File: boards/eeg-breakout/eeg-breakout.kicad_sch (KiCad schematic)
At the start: 36 parts, among them J1 Isolated SPI, J2 Electrodes, U1 ISOW7741, U2 ADS1292IRSMR

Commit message: feat: tweak the eeg breakout
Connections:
- net +3V3: now also U2.31 (RESP_MODP/IN3P), U2.32 (RESP_MODN_IN3N)
- net IN1N: now also C20.1, R6.1; no longer C22.1, R8.1, U2.32 (RESP_MODN_IN3N), U2.5 (IN2N)
- net IN2P: now also C21.1, R7.1; no longer C20.1, R6.1
- net EEG_BIAS renamed BIAS
- net EEG_C4 renamed CH1_N
- net CH1_N: now also J2.4 (Pin_4); no longer J2.2 (Pin_2)
- net EEG_F4 renamed CH1_P
- net EEG_M1 renamed CH2_N
- net CH2_N: now also J2.2 (Pin_2); no longer J2.1 (Pin_1)
- net EEG_O2 renamed CH2_P
- net CH2_P: now also J2.1 (Pin_1); no longer J2.4 (Pin_4)
- removed net IN3P: C21.1, R7.1, U2.31 (RESP_MODP/IN3P)
- new net IN2N: C22.1, R8.1, U2.5 (IN2N)
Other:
- title: OpenPSG EEG Analog Frontend -> OpenPSG EEG Breakout
- moved on the sheet: C19, C20, C21, C22, J2, R5, R6, R7, R8

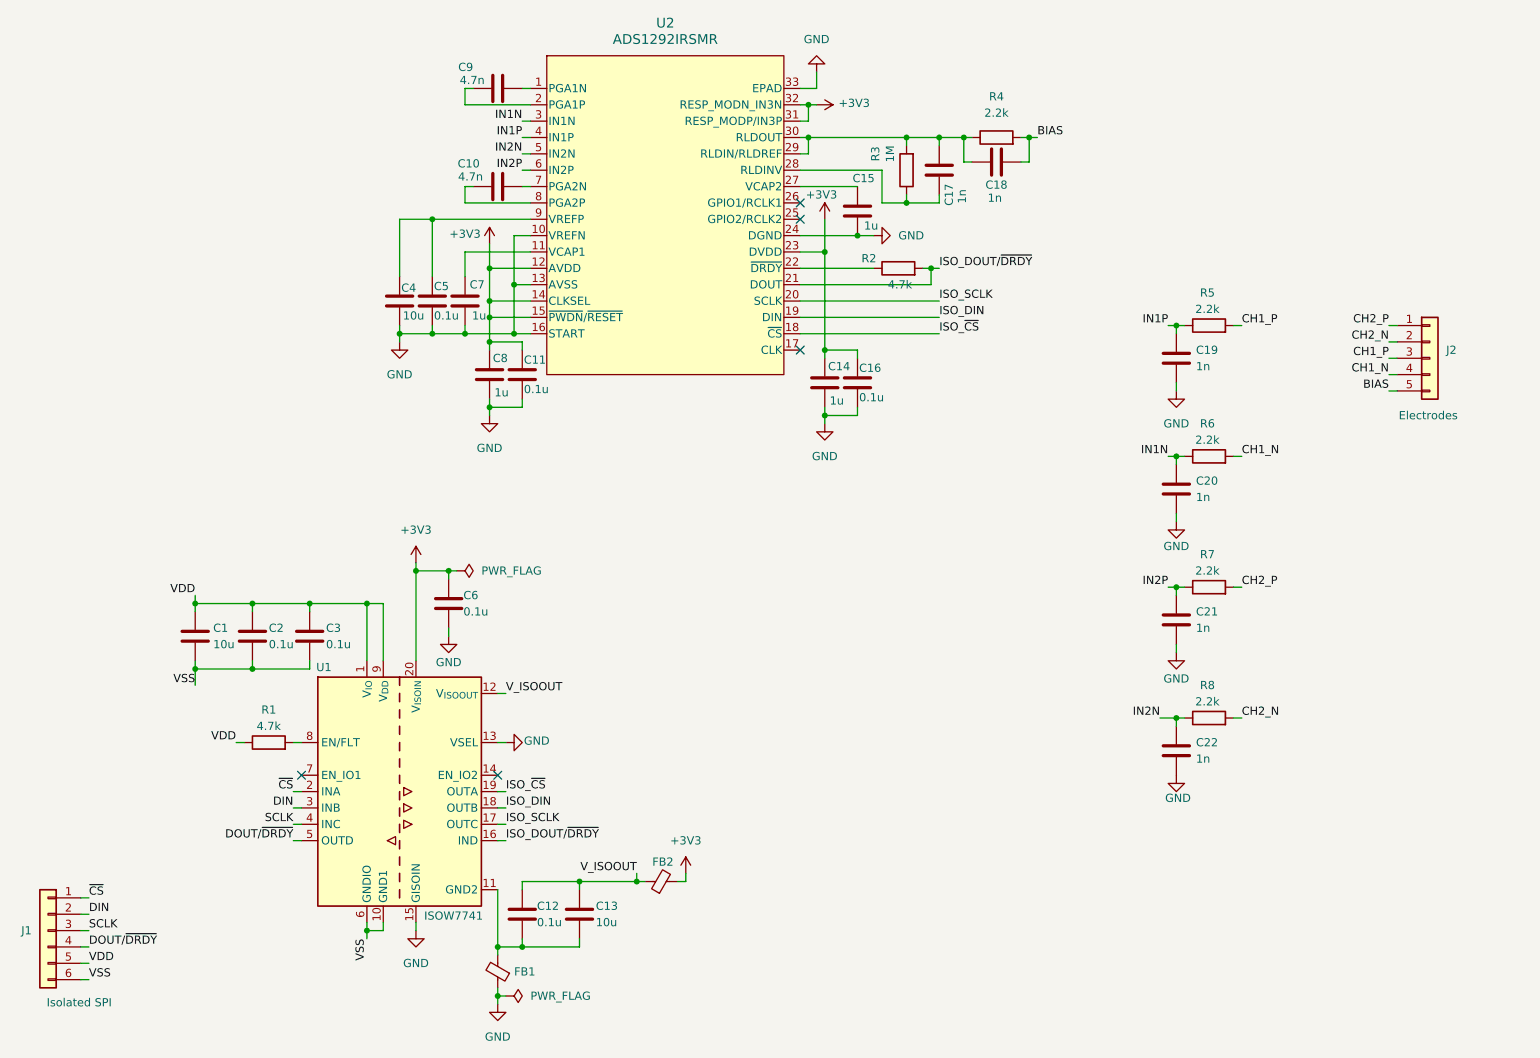
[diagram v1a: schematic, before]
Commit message: refactor: improve ads1292 breakout
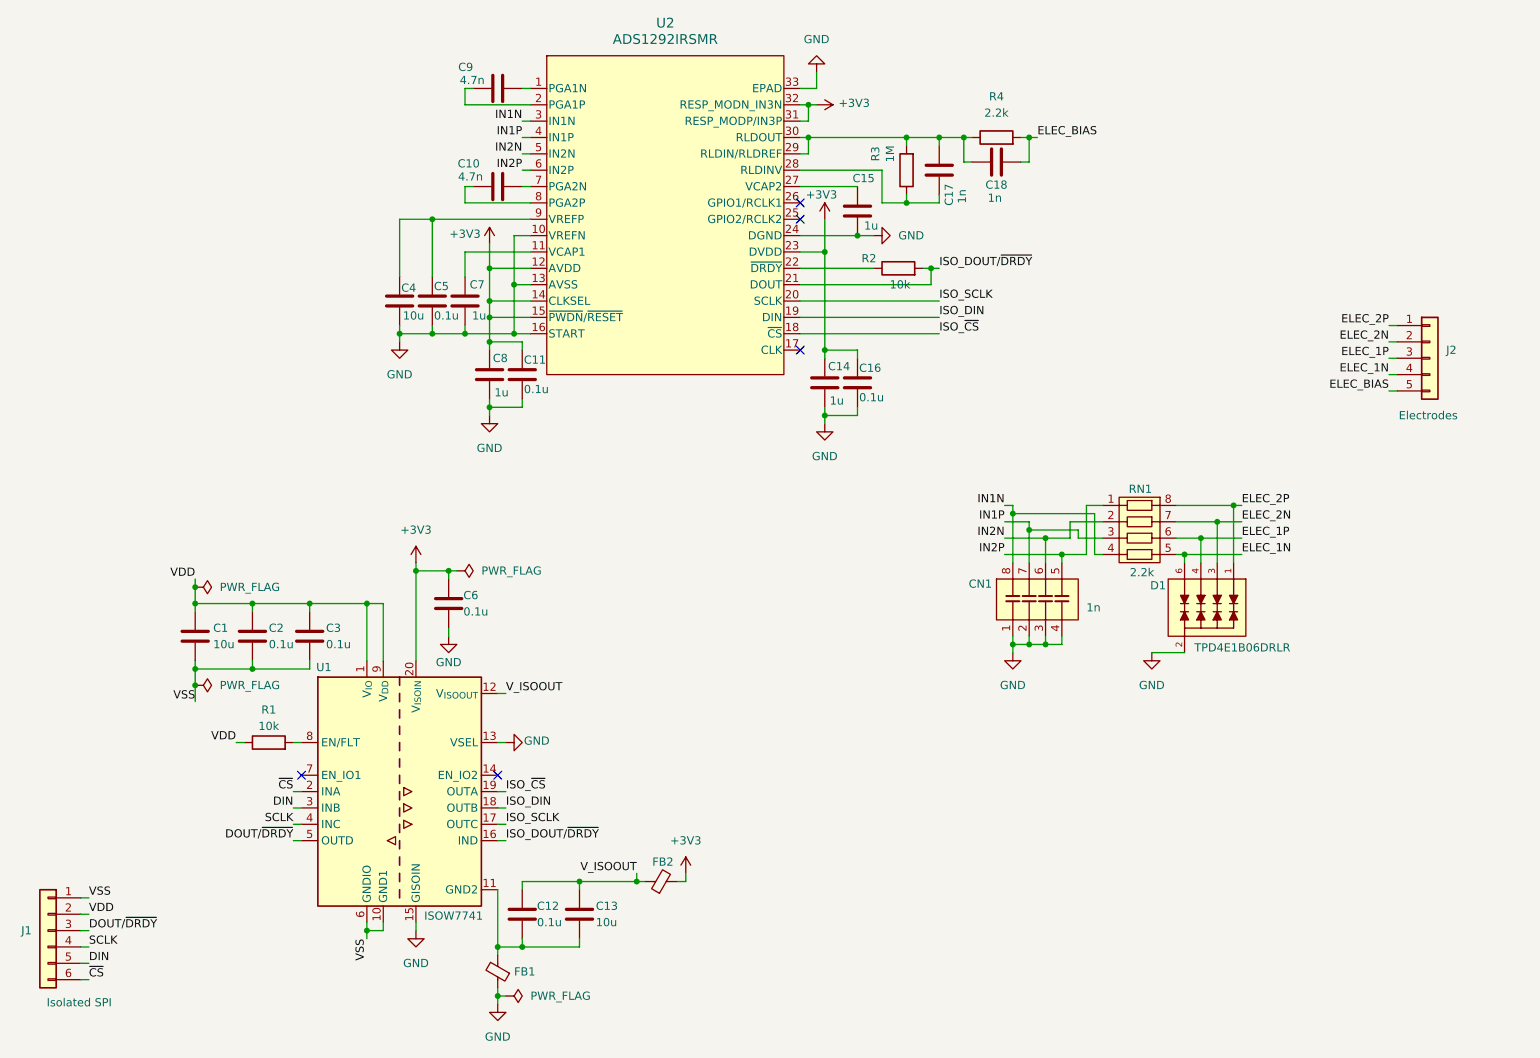
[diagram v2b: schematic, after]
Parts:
- removed C19, C20, C21, C22: 1n, Capacitor_SMD:C_0402_1005Metric, symbol Device:C
- removed R5, R6, R7, R8: 2.2k, Resistor_SMD:R_0402_1005Metric, symbol Device:R
- added CN1: 1n, Resistor_SMD:R_Array_Convex_4x0612, symbol C_Network_0612:C_Network_0612
- added D1: TPD4E1B06DRLR, Package_TO_SOT_SMD:SOT-563, symbol TPD4E1B06DRLR:TPD4E1B06DRLR
- added RN1: 2.2k, Resistor_SMD:R_Array_Convex_4x0402, symbol R_Network_0402x4:R_Network_0402x4
- J1: footprint Connector_PinHeader_1.00mm:PinHeader_1x06_P1.00mm_Vertical -> Connector_PinHeader_2.54mm:PinHeader_1x06_P2.54mm_Horizontal
- J2: footprint Connector_PinHeader_1.00mm:PinHeader_1x05_P1.00mm_Vertical -> Connector_PinHeader_2.54mm:PinHeader_1x05_P2.54mm_Horizontal
- R1, R2: value 4.7k -> 10k; LCSC PN C25900 -> C25744
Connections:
- net DIN: now also J1.5 (Pin_5); no longer J1.2 (Pin_2)
- net DOUT/~{DRDY}: now also J1.3 (Pin_3); no longer J1.4 (Pin_4)
- net GND: now also CN1.1, CN1.2, CN1.3, CN1.4, D1.2
- net IN1N: now also CN1.8, RN1.4
- net IN1P: now also CN1.7, RN1.3
- net IN2N: now also CN1.6, RN1.2
- net IN2P: now also CN1.5, RN1.1
- net SCLK: now also J1.4 (Pin_4); no longer J1.3 (Pin_3)
- net VDD: now also J1.2 (Pin_2); no longer J1.5 (Pin_5)
- net VSS: now also J1.1 (Pin_1); no longer J1.6 (Pin_6)
- net ~{CS}: now also J1.6 (Pin_6); no longer J1.1 (Pin_1)
- net BIAS renamed ELEC_BIAS
- net CH1_N renamed ELEC_1N
- net ELEC_1N: now also D1.6, RN1.5
- net CH1_P renamed ELEC_1P
- net ELEC_1P: now also D1.4, RN1.6
- net CH2_N renamed ELEC_2N
- net ELEC_2N: now also D1.3, RN1.7
- net CH2_P renamed ELEC_2P
- net ELEC_2P: now also D1.1, RN1.8
